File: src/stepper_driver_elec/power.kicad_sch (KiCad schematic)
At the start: 32 parts, among them J201 XT30, U201 MP2459GJ-Z-MS, U202 AP62200TWU, U203 HX4002

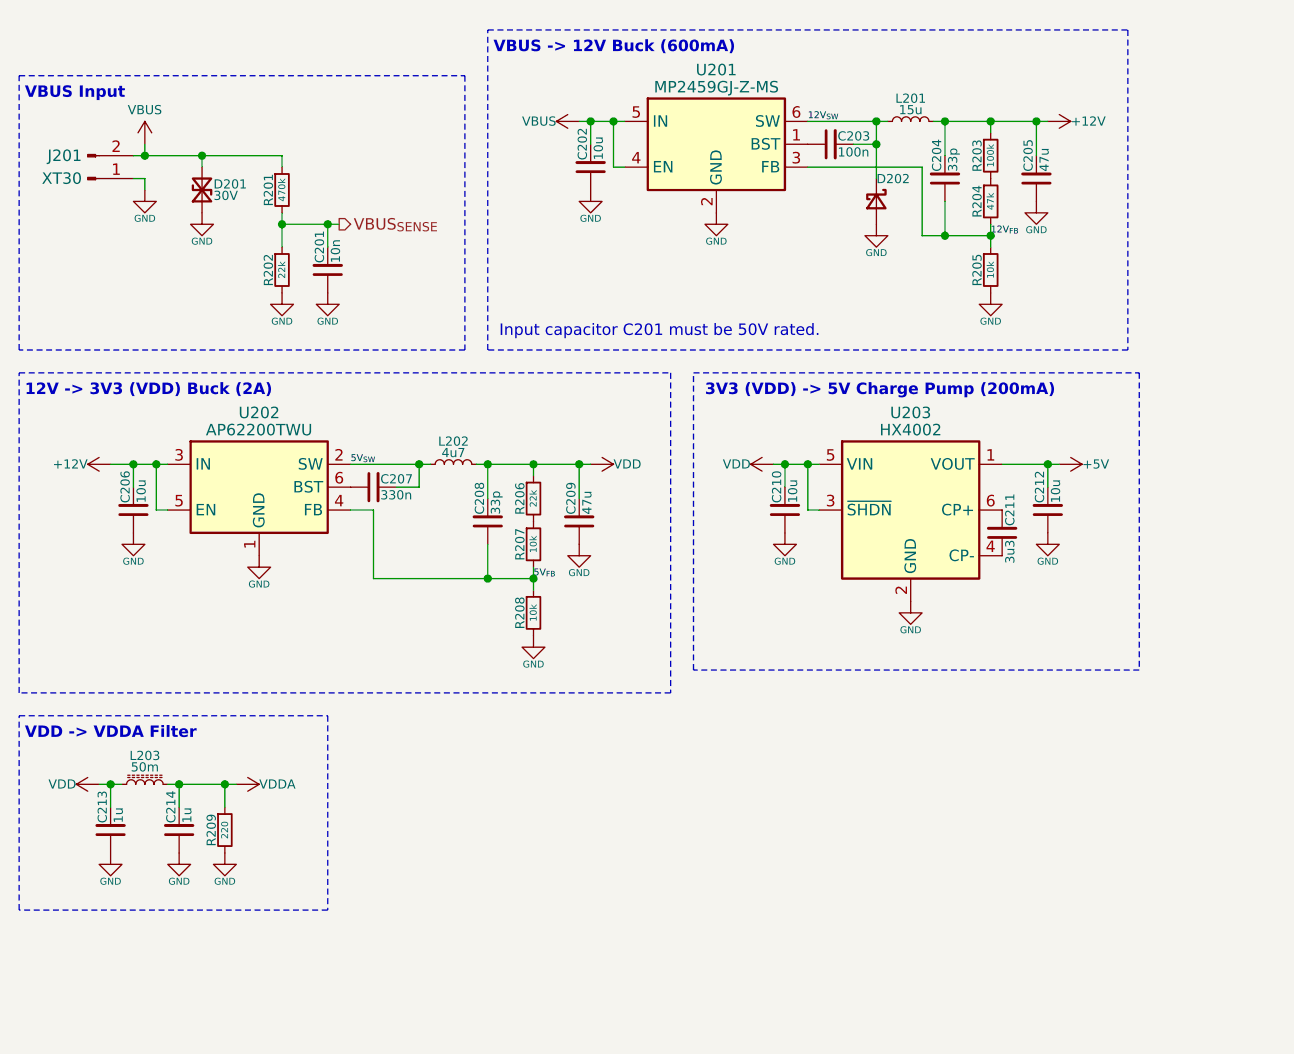
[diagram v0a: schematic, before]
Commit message: Correct capacitor selection and net labelling
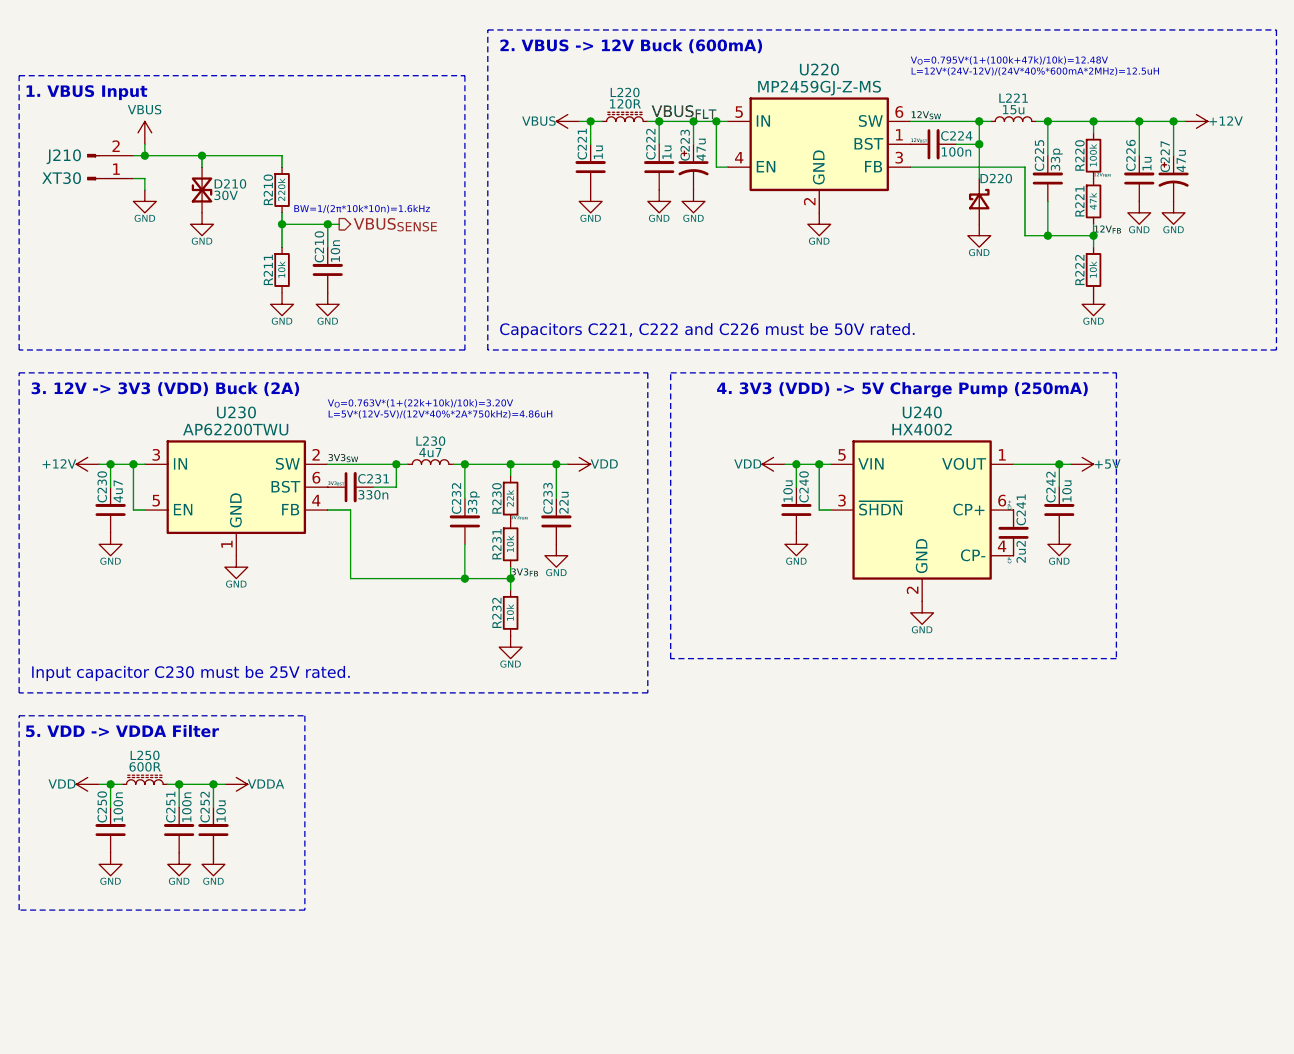
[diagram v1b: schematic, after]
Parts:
- removed C202: 10u, symbol Bluesat:C_CompactV
- removed C205: 47u, symbol Bluesat:C_CompactV
- removed R209: 220, symbol Bluesat:R_CompactV
- added C221, C222, C226: 1u, symbol Bluesat:C_CompactV
- added C223, C227: 47u, symbol Device:C_Polarized_Small_US
- added C252: 10u, symbol Bluesat:C_CompactV
- added L220: 120R, symbol Device:L_Ferrite_Small
- C230: renamed from C206; value 10u -> 4u7
- C233: renamed from C209; value 47u -> 22u
- C241: renamed from C211; value 3u3 -> 2u2
- C250: renamed from C213; value 1u -> 100n
- C251: renamed from C214; value 1u -> 100n
- L250: renamed from L203; value 50m -> 600R
- R210: renamed from R201; value 470k -> 220k
- R211: renamed from R202; value 22k -> 10k
- renumbered C201 to C210, C203 to C224, C204 to C225, C207 to C231, C208 to C232, C210 to C240, C212 to C242, D201 to D210, D202 to D220, J201 to J210, L201 to L221, L202 to L230, R203 to R220, R204 to R221, R205 to R222, R206 to R230, R207 to R231, R208 to R232, U201 to U220, U202 to U230, U203 to U240
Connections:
- net +12V: now also C226.2, C227.1
- net GND: now also C221.1, C222.1, C223.2, C226.1, C227.2, C252.1
- net VBUS: now also C221.2, L220.1; no longer U220.4 (EN), U220.5 (IN)
- net VDDA: now also C252.2
- net 12V_{FBM}: now reaches R220.2, R221.1
- net 12V_{BST}: now reaches C224.1, U220.1 (BST)
- net CP-: now reaches C241.1, U240.4 (CP-)
- net CP+: now reaches C241.2, U240.6 (CP+)
- net 3V3_{FBM}: now reaches R230.2, R231.1
- net 3V3_{BST}: now reaches C231.1, U230.6 (BST)
- net 5V_{FB} renamed 3V3_{FB}
- net 5V_{SW} renamed 3V3_{SW}
- new net VBUS_{FLT}: C222.2, C223.1, L220.2, U220.4 (EN), U220.5 (IN)
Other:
- note added: "1. VBUS Input"
- note added: "2. VBUS -> 12V Buck (600mA)"
- note added: "3. 12V -> 3V3 (VDD) Buck (2A)"
- note added: "4. 3V3 (VDD) -> 5V Charge Pump (250mA)"
- note added: "5. VDD -> VDDA Filter"
- note added: "BW=1/(2π*10k*10n)=1.6kHz"
- note added: "Capacitors C221, C222 and C226 must be 50V rated."
- note added: "Input capacitor C230 must be 25V rated."
- note added: "V_{O}=0.763V*(1+(22k+10k)/10k)=3.20V L=5V*(12V-5V)/(12V*40%*2A*750kHz)=4.86uH"
- note added: "V_{O}=0.795V*(1+(100k+47k)/10k)=12.48Vr L=12V*(24V-12V)/(24V*40%*600mA*2MHz)=12.5uH"
- note removed: "12V -> 3V3 (VDD) Buck (2A)"
- note removed: "3V3 (VDD) -> 5V Charge Pump (200mA)"
- note removed: "Input capacitor C201 must be 50V rated."
- note removed: "VBUS -> 12V Buck (600mA)"
- note removed: "VBUS Input"
- note removed: "VDD -> VDDA Filter"
- moved on the sheet: C224, C225, C230, C231, C232, C233, C240, C241, C242, D220, L221, L230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

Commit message: Create most of the top level schematic
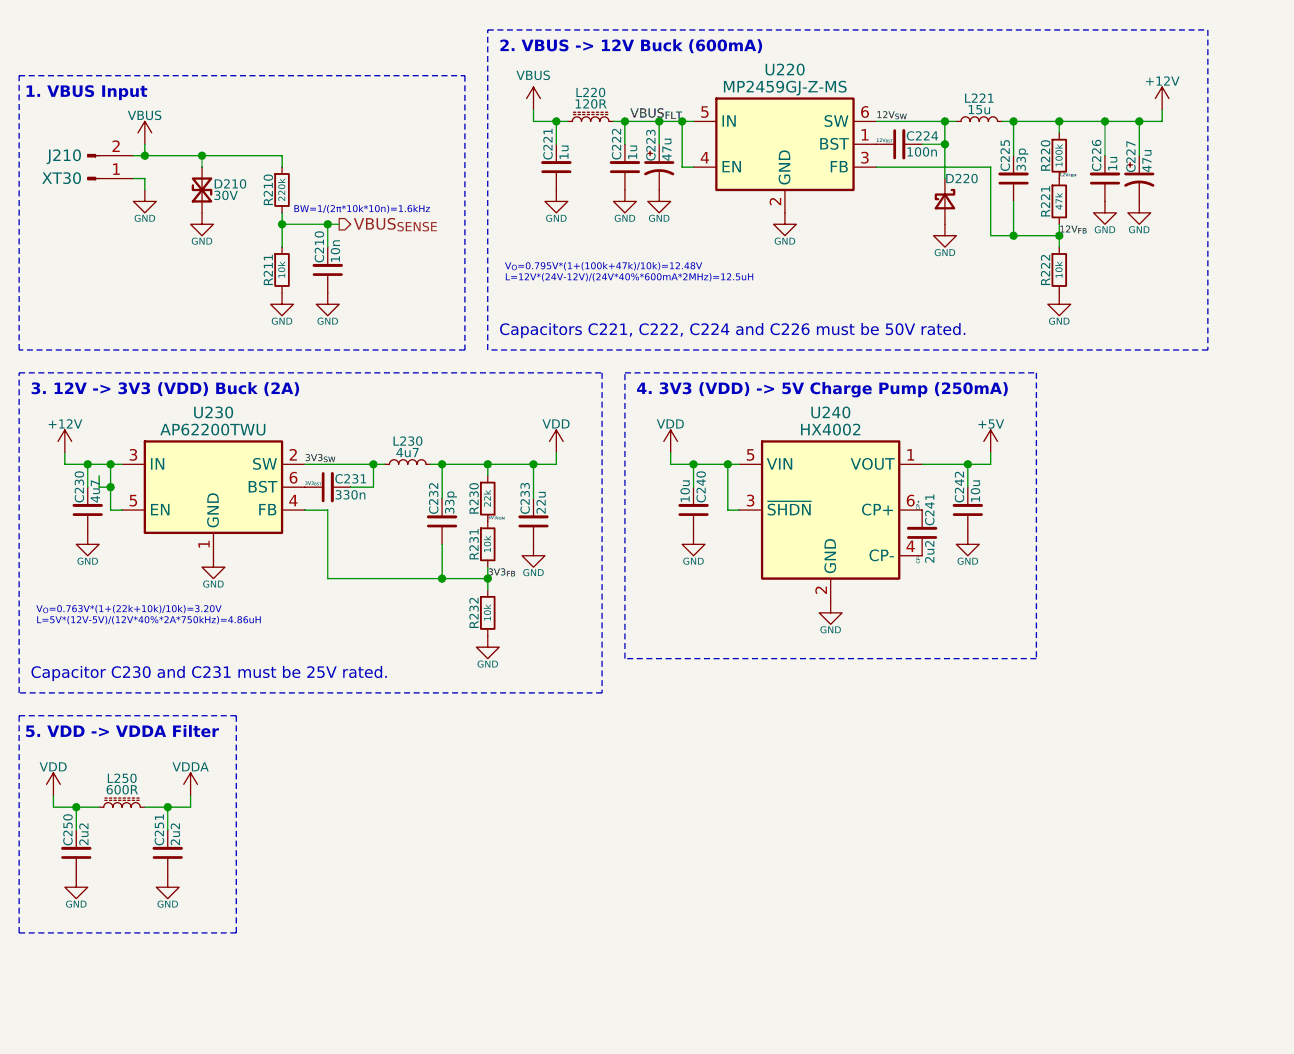
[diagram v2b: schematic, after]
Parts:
- removed C252: 10u, symbol Bluesat:C_CompactV
- C250, C251: value 100n -> 2u2
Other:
- note added: "Capacitor C230 and C231 must be 25V rated."
- note added: "Capacitors C221, C222, C224 and C226 must be 50V rated."
- note removed: "Capacitors C221, C222 and C226 must be 50V rated."
- note removed: "Input capacitor C230 must be 25V rated."
- moved on the sheet: C221, C222, C223, C224, C225, C226, C227, C230, C231, C232, C233, C240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

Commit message: IMPERIAL SCUM
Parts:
- C210, C224, C225, C232: footprint (none) -> Capacitor_SMD:C_0402_1005Metric
- C221, C222, C230, C240, C242: footprint (none) -> Capacitor_SMD:C_1206_3216Metric
- C223, C227: value 47u -> 68u; footprint (none) -> Capacitor_SMD:CP_Elec_6.3x7.7
- C226: footprint (none) -> Capacitor_SMD:C_0805_2012Metric
- C231: value 330n -> 220n; footprint (none) -> Capacitor_SMD:C_0402_1005Metric
- C233: footprint (none) -> Capacitor_SMD:C_1210_3225Metric
- C241, C250, C251: footprint (none) -> Capacitor_SMD:C_0603_1608Metric
- D210: footprint (none) -> Diode_SMD:D_SMF
- D220: footprint (none) -> Diode_SMD:D_SOD-123
- J210: value XT30 -> XT30M; footprint (none) -> Connector_AMASS:AMASS_XT30PW-M_1x02_P2.50mm_Horizontal
- L220: footprint (none) -> Resistor_SMD:R_0603_1608Metric
- L221: footprint (none) -> Inductor_SMD:L_Changjiang_FNR5040S
- L230: footprint (none) -> Inductor_SMD:L_Changjiang_FNR4020S
- L250, R210, R211, R220, R221, R222, R230, R231, R232: footprint (none) -> Resistor_SMD:R_0402_1005Metric
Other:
- note added: "Capacitor C230 must be 25V rated."
- note added: "Capacitors C221 and C222 must be 50V rated. Capacitors C224 and C226 must be 25V rated."
- note removed: "Capacitor C230 and C231 must be 25V rated."
- note removed: "Capacitors C221, C222, C224 and C226 must be 50V rated."

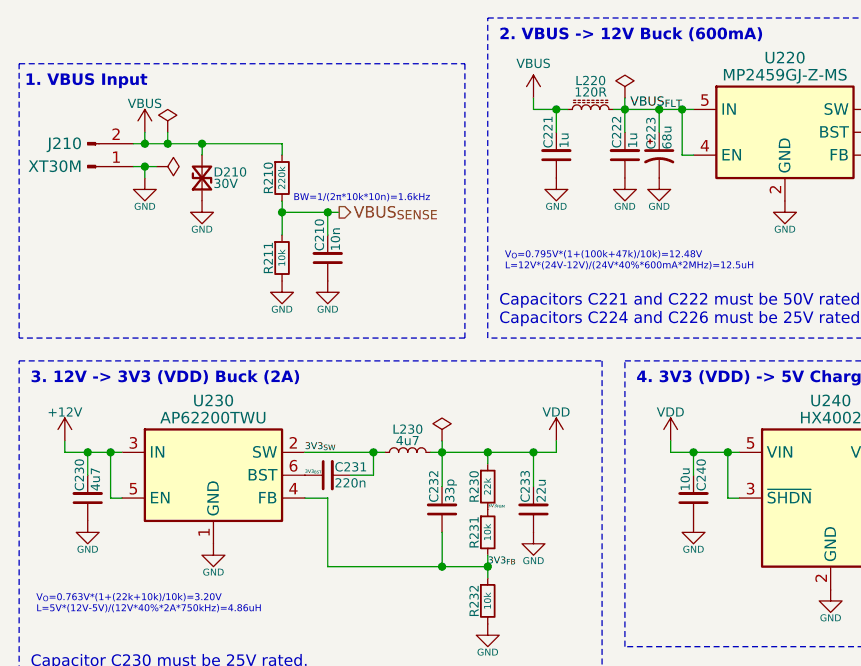
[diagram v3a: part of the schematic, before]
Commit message: Resolve issues on the stepper board found in initial testing
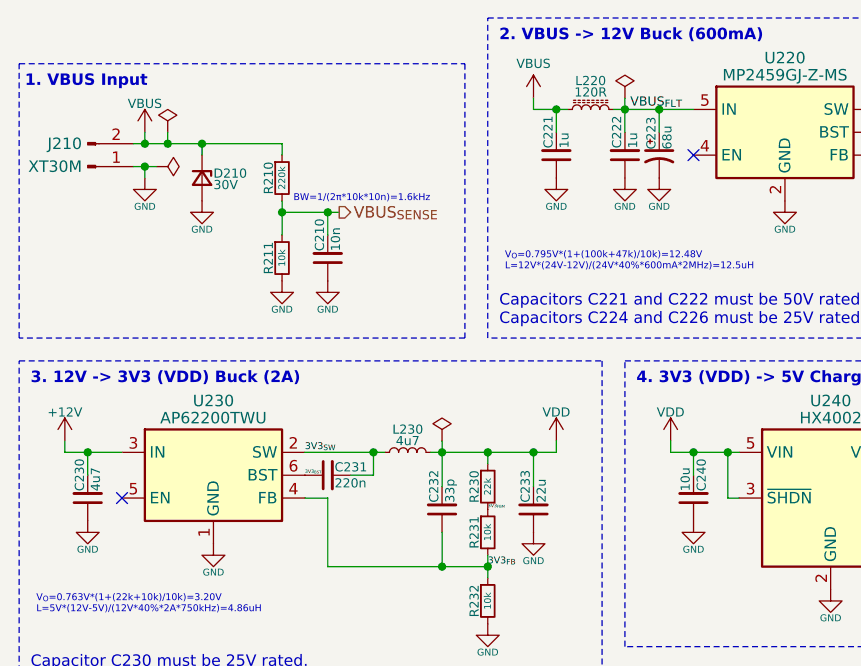
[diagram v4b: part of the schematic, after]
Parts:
- removed D210: 30V, Diode_SMD:D_SMF, symbol Device:D_TVS_Small
- added D210: 30V, Diode_SMD:D_SOD-123F, symbol Device:D_Zener_Small
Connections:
- net +12V: no longer U230.5 (EN)
- net GND: now also D210.2 (A)
- net VBUS: now also D210.1 (K)
- net VBUS_{FLT}: no longer U220.4 (EN)
- no-connect marks 0 -> 2
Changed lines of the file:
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@@
-	)
-	(junction
-		(at 88.9 27.94)
-		(diameter 0)
-		(color 0 0 0 0)
 	)
 	(junction
@@
 	)
 	(junction
-		(at 25.4 66.04)
-		(diameter 0)
-		(color 0 0 0 0)
-	)
-	(junction
 		(at 44.45 39.37)
 		(diameter 0)
@@
 		(color 0 0 0 0)
 	)
+	(no_connect
+		(at 90.17 33.02)
+	)
+	(no_connect
+		(at 26.67 71.12)
+	)
 	(wire
 		(pts
@@
 	(wire
 		(pts
-			(xy 26.67 71.12) (xy 25.4 71.12)
-		)
-		(stroke
-			(width 0)
-			(type default)
-		)
-	)
-	(wire
-		(pts
 			(xy 118.11 30.48) (xy 118.11 34.29)
 		)
@@
 	(wire
 		(pts
-			(xy 88.9 27.94) (xy 90.17 27.94)
-		)
-		(stroke
-			(width 0)
-			(type default)
-		)
-	)
-	(wire
-		(pts
 			(xy 19.05 104.14) (xy 21.59 104.14)
 		)
@@
 	(wire
 		(pts
-			(xy 25.4 66.04) (xy 26.67 66.04)
+			(xy 22.86 66.04) (xy 26.67 66.04)
 		)
 		(stroke
@@
 	(wire
 		(pts
-			(xy 90.17 33.02) (xy 88.9 33.02)
-		)
-		(stroke
-			(width 0)
-			(type default)
-		)
-	)
-	(wire
-		(pts
 			(xy 72.39 69.85) (xy 72.39 66.04)
 		)
@@
 	(wire
 		(pts
-			(xy 88.9 27.94) (xy 86.36 27.94)
+			(xy 86.36 27.94) (xy 90.17 27.94)
 		)
 		(stroke
@@
 	(wire
 		(pts
-			(xy 25.4 66.04) (xy 25.4 71.12)
-		)
-		(stroke
-			(width 0)
-			(type default)
-		)
-	)
-	(wire
-		(pts
 			(xy 46.99 66.04) (xy 54.61 66.04)
 		)
@@
 	(wire
 		(pts
-			(xy 22.86 66.04) (xy 25.4 66.04)
-		)
-		(stroke
-			(width 0)
-			(type default)
-		)
-	)
-	(wire
-		(pts
 			(xy 29.21 31.75) (xy 31.75 31.75)
 		)
@@
 		(pts
 			(xy 72.39 27.94) (xy 72.39 26.67)
-		)
-		(stroke
-			(width 0)
-			(type default)
-		)
-	)
-	(wire
-		(pts
-			(xy 88.9 27.94) (xy 88.9 33.02)
 		)
 		(stroke
@@
 	)
 	(symbol
-		(lib_id "Device:D_TVS_Small")
-		(at 35.56 35.56 90)
-		(unit 1)
-		(exclude_from_sim no)
-		(in_bom yes)
-		(on_board yes)
-		(dnp no)
-		(property "Reference" "D210"
-			(at 36.83 34.925 90)
-			(effects
-				(font
-					(size 1.016 1.016)
-				)
-				(justify right)
-			)
-		)
-		(property "Value" "30V"
-			(at 36.83 36.195 90)
-			(effects
-				(font
-					(size 1.016 1.016)
-				)
-				(justify right)
-			)
-		)
-		(property "Footprint" "Diode_SMD:D_SMF"
-			(at 35.56 35.56 0)
-			(effects
-				(font
-					(size 1.27 1.27)
-				)
-				(hide yes)
-			)
-		)
-		(property "Datasheet" "~"
-			(at 35.56 35.56 0)
-			(effects
-				(font
-					(size 1.27 1.27)
-				)
-				(hide yes)
-			)
-		)
-		(property "Description" "Bidirectional transient-voltage-suppression diode, small symbol"
-			(at 35.56 35.56 0)
-			(effects
-				(font
-					(size 1.27 1.27)
-				)
-				(hide yes)
-			)
-		)
-		(pin "1"
-		)
-		(pin "2"
-		)
-		(instances
-			(project ""
-				(path "/22ad96d7-4eff-4ee6-90ff-f4a9952d1282/15b35f53-66e8-4f33-b39d-ce4effc92c20"
-					(reference "D210")
-					(unit 1)
-				)
-			)
-		)
-	)
-	(symbol
 		(lib_id "power:+12V")
 		(at 20.32 64.77 0)
@@
 					(unit 1)
 				)
+			)
+		)
+	)
+	(symbol
+		(lib_id "Device:D_Zener_Small")
+		(at 35.56 35.56 270)
+		(unit 1)
+		(exclude_from_sim no)
+		(in_bom yes)
+		(on_board yes)
+		(dnp no)
+		(property "Reference" "D210"
+			(at 36.83 35.052 90)
+			(effects
+				(font
+					(size 1.016 1.016)
+				)
+				(justify left)
+			)
+		)
+		(property "Value" "30V"
+			(at 36.83 36.322 90)
+			(effects
+				(font
+					(size 1.016 1.016)
+				)
+				(justify left)
+			)
+		)
+		(property "Footprint" "Diode_SMD:D_SOD-123F"
+			(at 35.56 35.56 90)
+			(effects
+				(font
+					(size 1.27 1.27)
+				)
+				(hide yes)
+			)
+		)
+		(property "Datasheet" "~"
+			(at 35.56 35.56 90)
+			(effects
+				(font
+					(size 1.27 1.27)
+				)
+				(hide yes)
+			)
+		)
+		(property "Description" "Zener diode, small symbol"
+			(at 35.56 35.56 0)
+			(effects
+				(font
+					(size 1.27 1.27)
+				)
+				(hide yes)
+			)
+		)
+		(pin "2"
+		)
+		(pin "1"
+		)
+		(instances
+			(project ""
+				(path "/22ad96d7-4eff-4ee6-90ff-f4a9952d1282/15b35f53-66e8-4f33-b39d-ce4effc92c20"
+					(reference "D210")
+					(unit 1)
+				)

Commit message: https://www.youtube.com/watch?v=6n3pFFPSlW4
I love ice coffee
stm32 is
a scary platform
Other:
- note added: "V_{O}=0.763V*(1+(22k+10k)/10k)=3.20V L=3.3V*(12V-3.3V)/(12V*35%*2A*750kHz)=4.56uH"
- note removed: "V_{O}=0.763V*(1+(22k+10k)/10k)=3.20V L=5V*(12V-5V)/(12V*40%*2A*750kHz)=4.86uH"
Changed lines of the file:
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@@
 		)
 	)
-	(text "V_{O}=0.763V*(1+(22k+10k)/10k)=3.20V\nL=5V*(12V-5V)/(12V*40%*2A*750kHz)=4.86uH"
+	(text "V_{O}=0.763V*(1+(22k+10k)/10k)=3.20V\nL=3.3V*(12V-3.3V)/(12V*35%*2A*750kHz)=4.56uH"
 		(exclude_from_sim no)
 		(at 17.145 81.915 0)

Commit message: Merg
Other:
- note added: "V_{O}=0.763V*(1+(22k+10k)/10k)=3.20V L=5V*(12V-5V)/(12V*40%*2A*750kHz)=4.86uH"
- note removed: "V_{O}=0.763V*(1+(22k+10k)/10k)=3.20V L=3.3V*(12V-3.3V)/(12V*35%*2A*750kHz)=4.56uH"
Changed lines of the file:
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@@
 		)
 	)
-	(text "V_{O}=0.763V*(1+(22k+10k)/10k)=3.20V\nL=3.3V*(12V-3.3V)/(12V*35%*2A*750kHz)=4.56uH"
+	(text "V_{O}=0.763V*(1+(22k+10k)/10k)=3.20V\nL=5V*(12V-5V)/(12V*40%*2A*750kHz)=4.86uH"
 		(exclude_from_sim no)
 		(at 17.145 81.915 0)

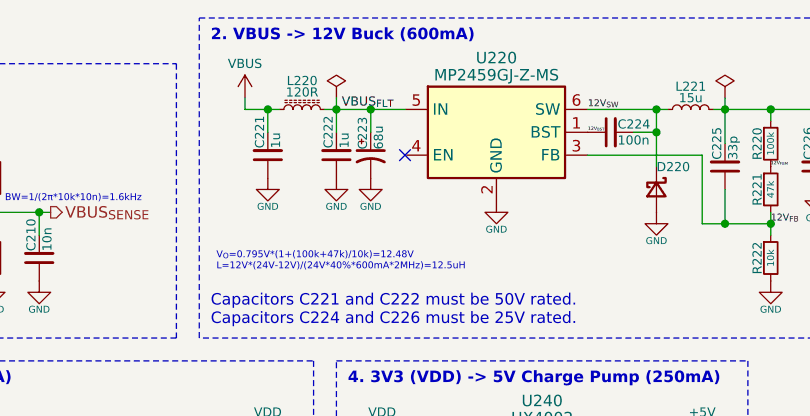
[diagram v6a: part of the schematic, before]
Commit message: [ELEC] Tie MP2459GJ EN pin to Vbus
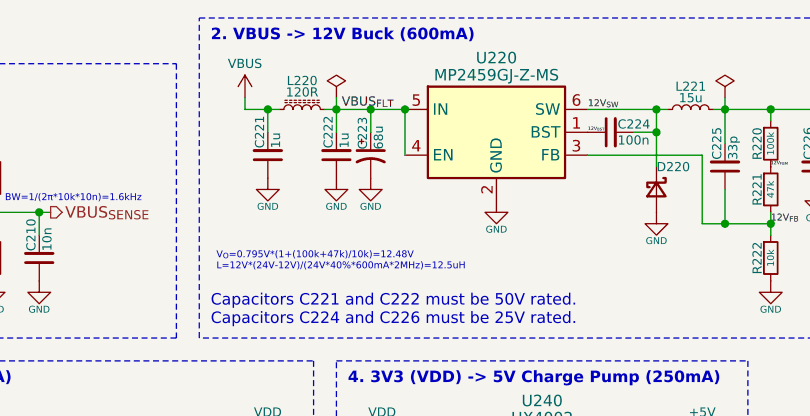
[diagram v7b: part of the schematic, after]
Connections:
- net VBUS_{FLT}: now also U220.4 (EN)
- no-connect marks 2 -> 1
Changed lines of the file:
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@@
+	)
+	(junction
+		(at 90.17 27.94)
+		(diameter 0)
+		(color 0 0 0 0)
 	)
 	(junction
@@
 		(diameter 0)
 		(color 0 0 0 0)
-	)
-	(no_connect
-		(at 90.17 33.02)
 	)
 	(no_connect
@@
 		)
 		(stroke
+			(width 0)
+			(type default)
+		)
+	)
+	(wire
+		(pts
+			(xy 90.17 27.94) (xy 90.17 33.02)
+		)
+		(stroke
